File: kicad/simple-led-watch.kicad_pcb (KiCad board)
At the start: 2 copper layers, 32.5 x 32.5 mm, 156 parts, among them P1 BATTERY, P3 USB_OTG, Q1 MMBT3904, Q2 MMBT3904, SW1 SPST-4PIN, SW2 SPST-4PIN, SW3 SPST-4PIN, SW4 SPST-4PIN, U1 MCP73832, U2 TPS62736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

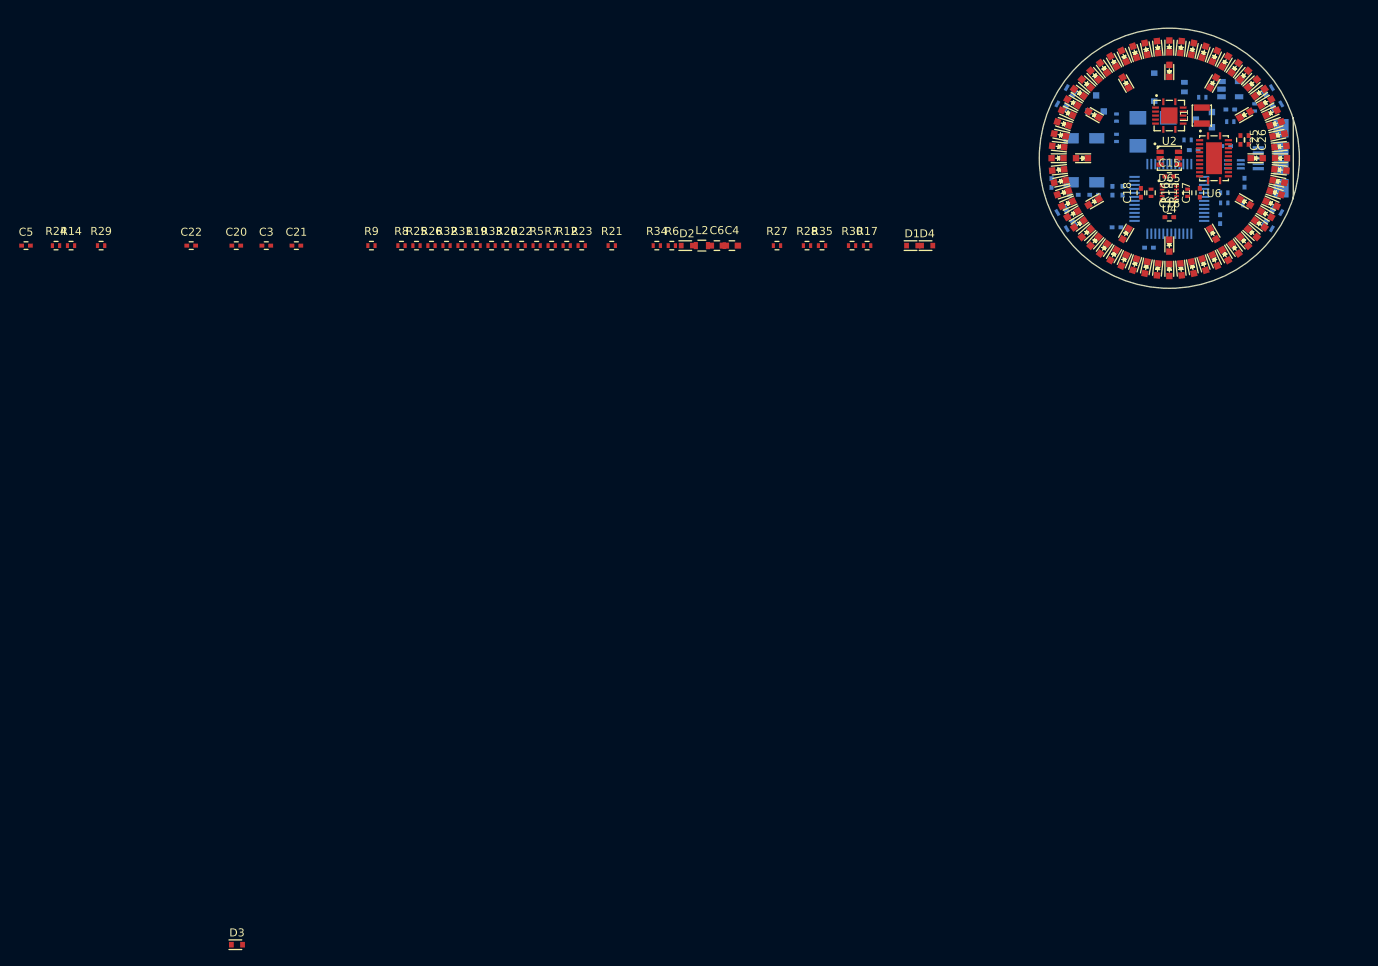
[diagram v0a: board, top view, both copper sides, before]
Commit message: Finished initial placement of all components
Got rid of several pullup resistors and unnecessary components.
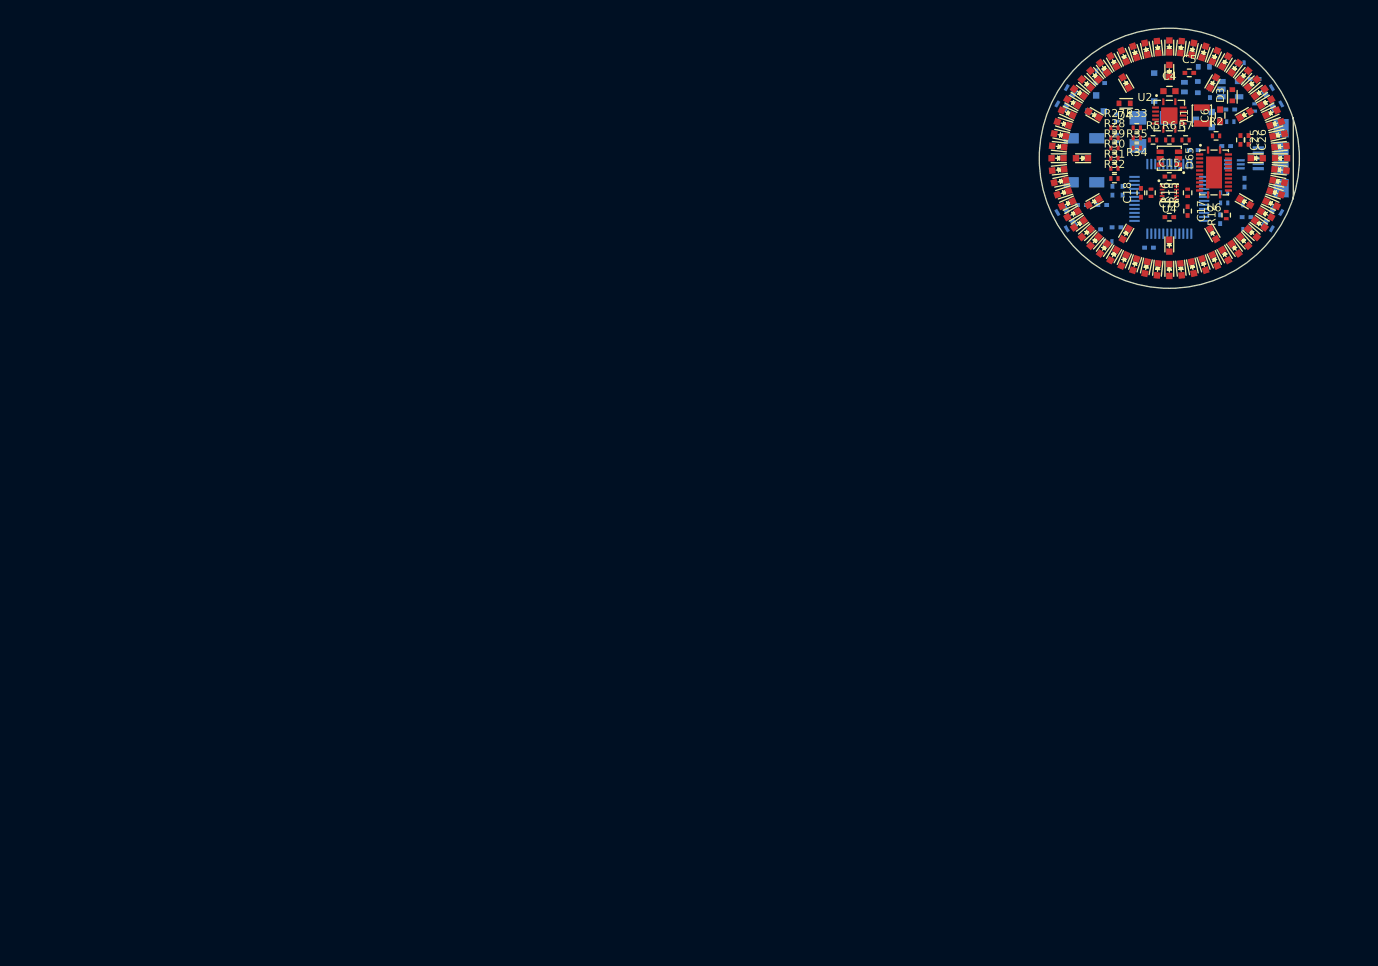
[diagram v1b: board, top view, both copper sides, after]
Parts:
- removed L2: 10u, Resistors_SMD:R_0603
- removed R14, R9: 0, Resistors_SMD:R_0402
- removed R17, R3: 10K, Resistors_SMD:R_0402
- removed R19, R21, R23, R25: R, Resistors_SMD:R_0402
- removed R8: 4M, Resistors_SMD:R_0402
- C20, C21, C22, C3, D1, D2: moved to B.Cu
- R2: value 10K -> 0; moved to F.Cu
- R20, R22, R24, R26: value R -> 0; moved to B.Cu
- R6: value 6M -> 0
- moved D3 163.6 mm to (173.0, 81.0), turned to 90 degrees
- moved C5 147.0 mm to (167.6, 78.2)
- moved R24 131.5 mm to (157.5, 99.3), turned to 180 degrees
- moved R29 127.3 mm to (158.2, 87.6)
- moved C20 126.3 mm to (174.8, 96.3)
- moved C3 119.5 mm to (170.2, 80.8), turned to 270 degrees
- moved C22 115.4 mm to (156.5, 79.5), turned to 180 degrees
- moved C21 100.0 mm to (156.0, 97.8), turned to 180 degrees
- moved R20 94.5 mm to (174.0, 77.0), turned to 180 degrees
- moved R22 90.6 mm to (174.8, 97.8)
- moved R26 86.4 mm to (156.5, 78.0), turned to 180 degrees
- moved R32 83.9 mm to (158.2, 91.4)
- moved R12 82.5 mm to (172.2, 96.0), turned to 90 degrees
- moved R31 82.2 mm to (158.2, 90.2)
- moved R33 82.0 mm to (161.0, 85.1)
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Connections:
- net /Control/STM32_OSC32_IN renamed /Control/STM32_OSC32+
- net /Control/STM32_OSC32_OUT renamed /Control/STM32_OSC32-
- C11 pad 1: /Control/STM32_VDDA -> +3V3
- C12 pad 1: /Control/STM32_VDDA -> +3V3
- C6 pad 1: +3V3 -> /Power Supply/+3.3V_REG_OUT
- D3 pad 1: +3V3 -> /Power Supply/+3.3V_REG_OUT
- L1 pad 2: +3V3 -> /Power Supply/+3.3V_REG_OUT
- R2 pad 2: /Control/CHG_STAT -> /Power Supply/+3.3V_REG_OUT
- R6 pad 1: /Power Supply/+3.3V_REG_VRDIV -> /Power Supply/+3.3V_REG_VOUT_SET
- R7 pad 1: /Power Supply/+3.3V_REG_VOUT_SET -> /Power Supply/+3.3V_REG_VOK_SET
- U2 pad 11: +3V3 -> /Power Supply/+3.3V_REG_OUT
- U2 pad 14: (no net) -> GND
- U2 pad 2: (no net) -> GND
- U2 pad 3: (no net) -> GND
- U2 pad 4: (no net) -> GND
- U3 pad 9: /Control/STM32_VDDA -> +3V3

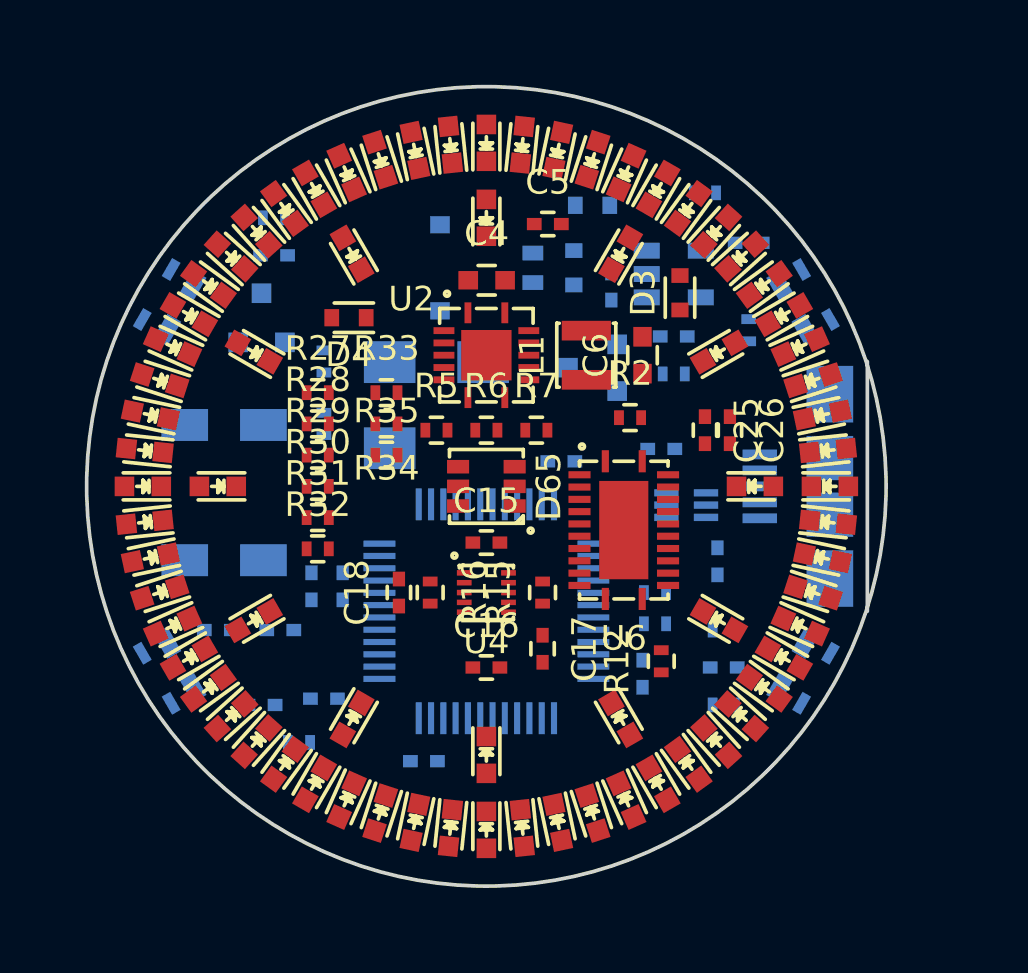
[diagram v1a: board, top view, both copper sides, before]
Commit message: Initial route of power and LED ring
I had to do the order swapping thing that I did on the last design
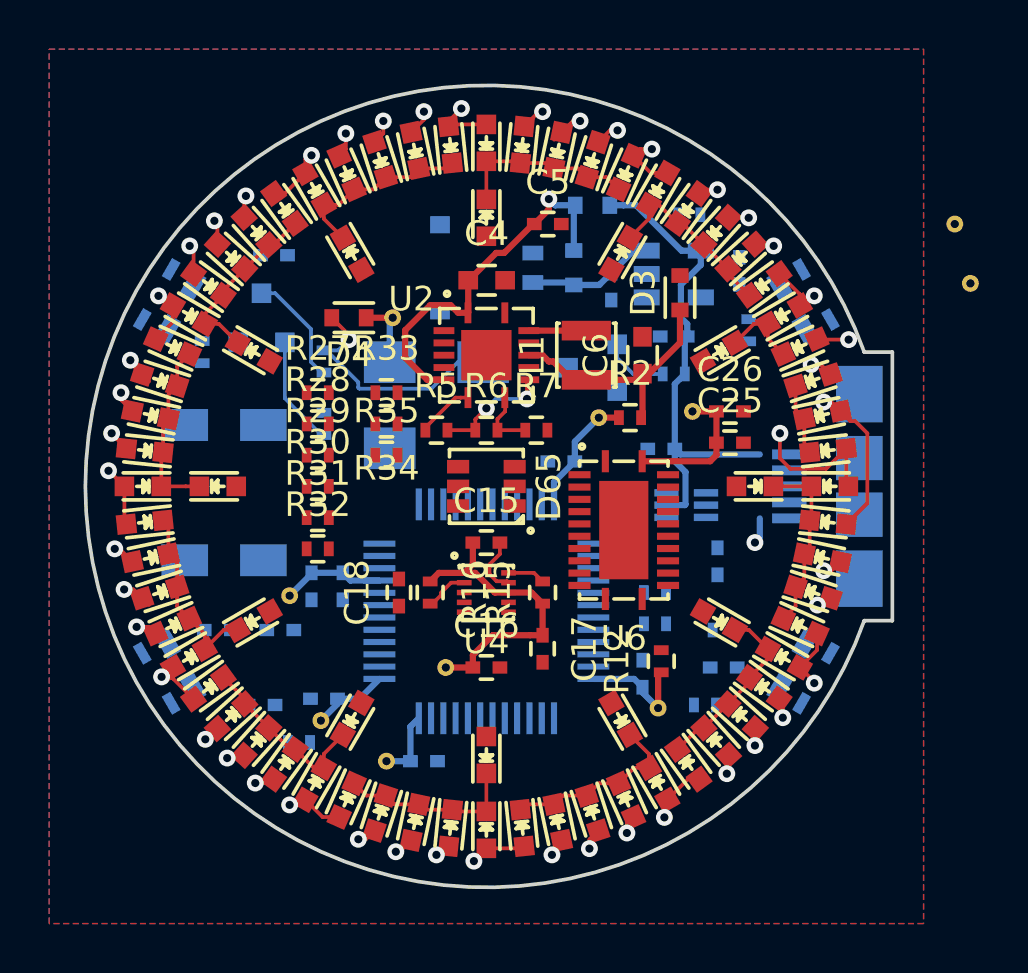
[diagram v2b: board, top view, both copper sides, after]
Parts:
- added REF**: 1PIN_VIA, simple-led-watch:1PIN_VIA, F.Cu at (169.7, 86.1)
- added REF**: 1PIN_VIA, simple-led-watch:1PIN_VIA, F.Cu at (161.3, 82.0)
- added REF**: 1PIN_VIA, simple-led-watch:1PIN_VIA, F.Cu at (184.8, 80.6)
- added REF**: 1PIN_VIA, simple-led-watch:1PIN_VIA, F.Cu at (184.2, 78.2)
- added REF**: 1PIN_VIA, simple-led-watch:1PIN_VIA, F.Cu at (172.1, 97.9)
- added REF**: 1PIN_VIA, simple-led-watch:1PIN_VIA, F.Cu at (161.0, 100.1)
- added REF**: 1PIN_VIA, simple-led-watch:1PIN_VIA, F.Cu at (158.4, 98.4)
- added REF**: 1PIN_VIA, simple-led-watch:1PIN_VIA, F.Cu at (163.4, 96.3)
- added REF**: 1PIN_VIA, simple-led-watch:1PIN_VIA, F.Cu at (157.1, 93.3)
- added REF**: 1PIN_VIA, simple-led-watch:1PIN_VIA, F.Cu at (173.5, 85.9)
- moved R26 6.19 mm to (153.5, 83.4), turned to 270 degrees
- moved C19 1.20 mm to (175.4, 80.1), turned to 270 degrees
- moved P3 1.20 mm to (180.3, 88.9)
- moved C25 1.14 mm to (175.0, 87.1), turned to 0 degrees
- moved R20 1.09 mm to (173.4, 77.9)
- moved C26 0.76 mm to (175.0, 85.9), turned to 0 degrees
- moved R22 0.76 mm to (174.0, 97.8)
- turned C22 to 0 degrees
- turned D66 to 270 degrees
- turned D67 to 240 degrees
- turned D68 to 210 degrees
- turned D69 to 180 degrees
- turned D70 to 150 degrees
- turned D71 to 120 degrees
- turned D72 to 90 degrees
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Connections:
- D10 pad 2: /LEDs/LED_A_R0 -> /LEDs/LED_A_R4
- D11 pad 2: /LEDs/LED_A_R1 -> /LEDs/LED_A_R3
- D13 pad 2: /LEDs/LED_A_R3 -> /LEDs/LED_A_R1
- D14 pad 2: /LEDs/LED_A_R4 -> /LEDs/LED_A_R0
- D20 pad 2: /LEDs/LED_A_R0 -> /LEDs/LED_A_R4
- D21 pad 2: /LEDs/LED_A_R1 -> /LEDs/LED_A_R3
- D23 pad 2: /LEDs/LED_A_R3 -> /LEDs/LED_A_R1
- D24 pad 2: /LEDs/LED_A_R4 -> /LEDs/LED_A_R0
- D30 pad 2: /LEDs/LED_A_R0 -> /LEDs/LED_A_R4
- D31 pad 2: /LEDs/LED_A_R1 -> /LEDs/LED_A_R3
- D33 pad 2: /LEDs/LED_A_R3 -> /LEDs/LED_A_R1
- D34 pad 2: /LEDs/LED_A_R4 -> /LEDs/LED_A_R0
- D40 pad 2: /LEDs/LED_A_R0 -> /LEDs/LED_A_R4
- D41 pad 2: /LEDs/LED_A_R1 -> /LEDs/LED_A_R3
- D43 pad 2: /LEDs/LED_A_R3 -> /LEDs/LED_A_R1
- D44 pad 2: /LEDs/LED_A_R4 -> /LEDs/LED_A_R0
- D50 pad 2: /LEDs/LED_A_R0 -> /LEDs/LED_A_R4
- D51 pad 2: /LEDs/LED_A_R1 -> /LEDs/LED_A_R3
- D53 pad 2: /LEDs/LED_A_R3 -> /LEDs/LED_A_R1
- D54 pad 2: /LEDs/LED_A_R4 -> /LEDs/LED_A_R0
- D60 pad 2: /LEDs/LED_A_R0 -> /LEDs/LED_A_R4
- D61 pad 2: /LEDs/LED_A_R1 -> /LEDs/LED_A_R3
- D63 pad 2: /LEDs/LED_A_R3 -> /LEDs/LED_A_R1
- D64 pad 2: /LEDs/LED_A_R4 -> /LEDs/LED_A_R0
- U5 pad 2: (no net) -> GND
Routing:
- net /LEDs/LED_A_R2: track 0.00 -> 103.8 mm, vias 0 -> 12
- net /LEDs/LED_A_R1: track 0.00 -> 101.2 mm, vias 0 -> 12
- net /LEDs/LED_A_R3: track 0.00 -> 99.5 mm, vias 0 -> 11
- net /LEDs/LED_A_R0: track 0.00 -> 96.2 mm, vias 0 -> 6
- net /LEDs/LED_A_R4: track 0.00 -> 94.4 mm, vias 0 -> 6
- net +3V3: track 0.00 -> 41.6 mm
- net /Power Supply/VUSB: track 0.00 -> 20.0 mm
- net /Power Supply/+3.3V_REG_SRC: track 0.00 -> 15.4 mm, vias 0 -> 1
- net /Power Supply/+3.3V_REG_OUT: track 0.00 -> 10.3 mm
- net Net-(D4-Pad2): track 0.00 -> 10.1 mm, vias 0 -> 1
- net /LEDs/LED_SEG5: track 0.00 -> 7.59 mm
- net /LEDs/LED_SEG8: track 0.00 -> 7.59 mm
- net /LEDs/LED_SEG11: track 0.00 -> 7.59 mm
- net /LEDs/LED_SEG6: track 0.00 -> 7.40 mm
- net /LEDs/LED_SEG9: track 0.00 -> 7.40 mm
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- added copper zone on In1.Cu, net +3V3
- added copper zone on B.Cu, net GND
- added copper zone on F.Cu, net GND
- added copper zone on In2.Cu, net GND
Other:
- board size 32.5 x 32.5 mm -> 32.8 x 32.6 mm
- copper layers 2 -> 4
- net class Default: clearance 0.2 -> 0.1524; trace_width 0.25 -> 0.1524
- net class Power added: clearance 0.1524, trace_width 0.254, via_dia 0.6858, via_drill 0.3302
- rule trace_clearance: 0.2 -> 0.1524
- board text added: "Notes: Vias MUST be tented since we put them beneath some metal components"

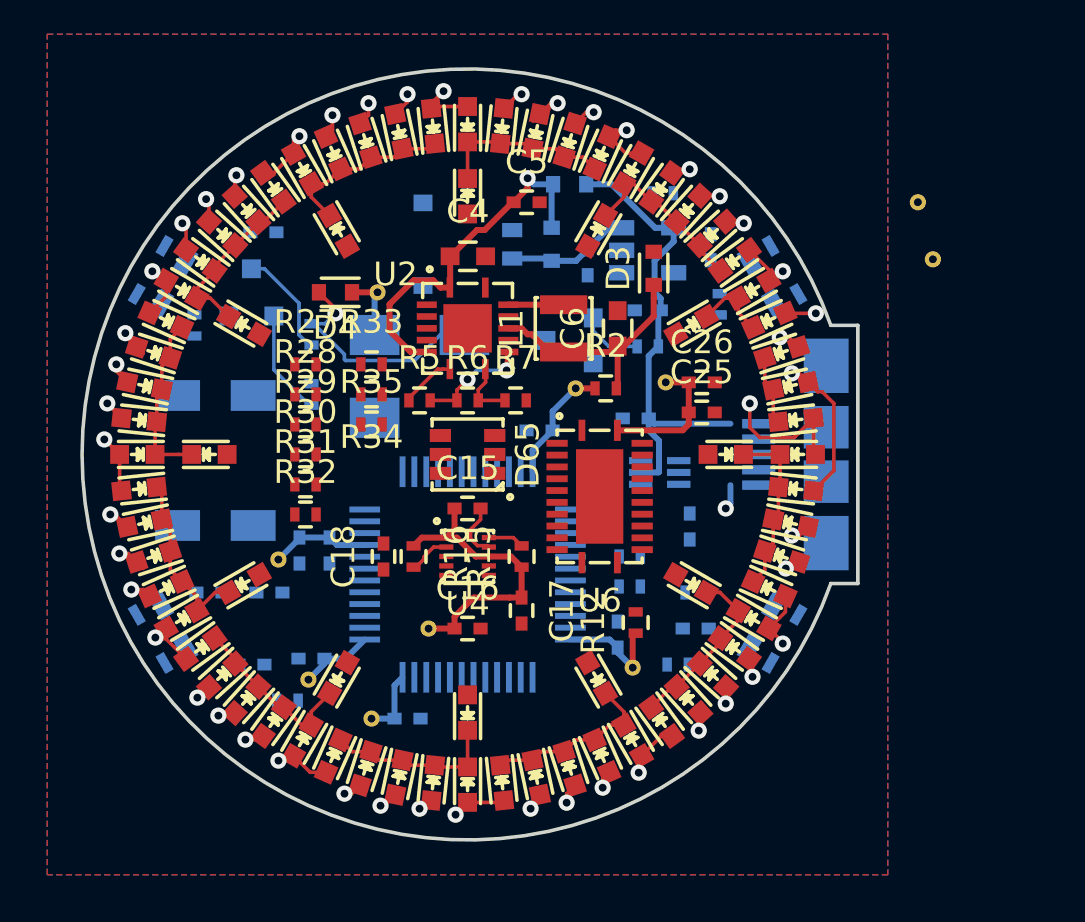
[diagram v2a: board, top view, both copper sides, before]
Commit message: Routed most of the board, except buttons and interrupts
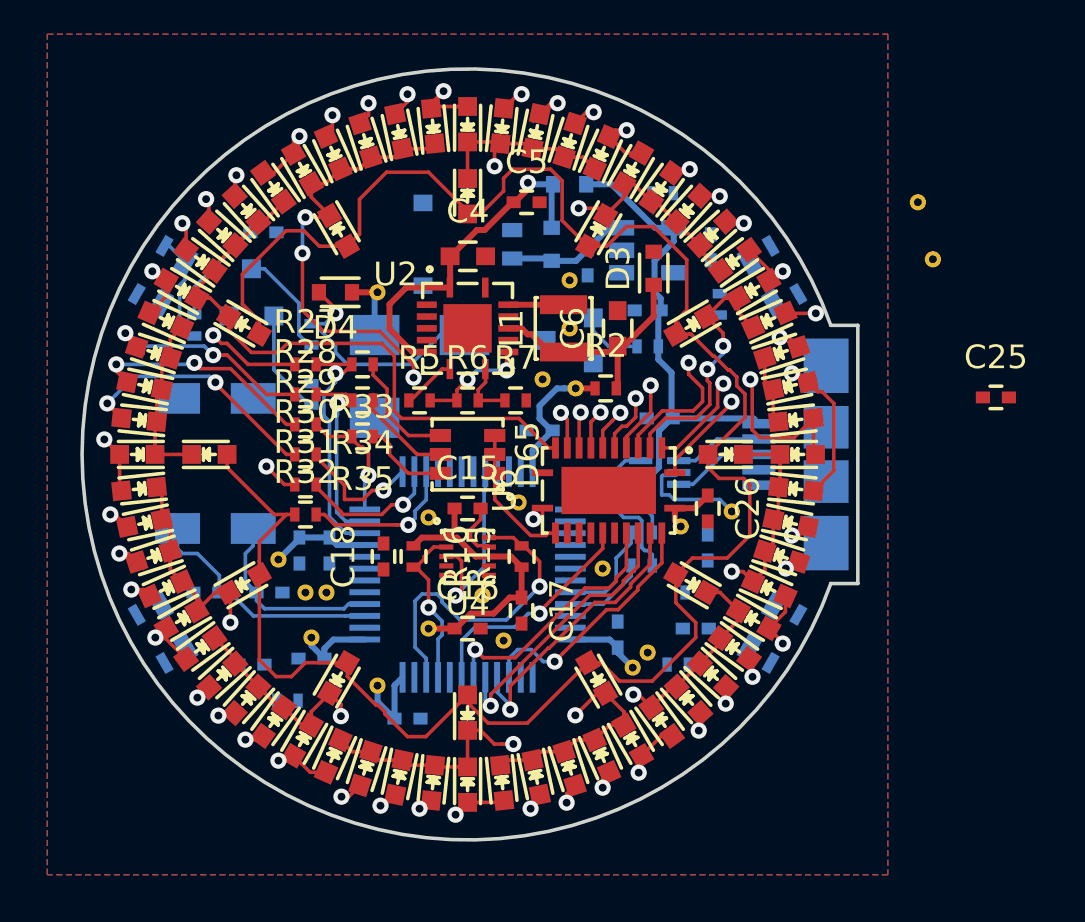
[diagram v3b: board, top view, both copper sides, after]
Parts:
- removed R12: 10K, Resistors_SMD:R_0402
- added REF**: 1PIN_VIA, simple-led-watch:1PIN_VIA, F.Cu at (172.7, 97.3)
- added REF**: 1PIN_VIA, simple-led-watch:1PIN_VIA, F.Cu at (167.3, 90.9)
- added REF**: 1PIN_VIA, simple-led-watch:1PIN_VIA, F.Cu at (159.1, 94.7)
- added REF**: 1PIN_VIA, simple-led-watch:1PIN_VIA, F.Cu at (158.2, 94.7)
- added REF**: 1PIN_VIA, simple-led-watch:1PIN_VIA, F.Cu at (170.8, 93.7)
- added REF**: 1PIN_VIA, simple-led-watch:1PIN_VIA, F.Cu at (163.4, 91.6)
- added REF**: 1PIN_VIA, simple-led-watch:1PIN_VIA, F.Cu at (166.6, 96.8)
- added REF**: 1PIN_VIA, simple-led-watch:1PIN_VIA, F.Cu at (165.7, 94.9)
- added REF**: 1PIN_VIA, simple-led-watch:1PIN_VIA, F.Cu at (169.4, 81.5)
- added REF**: 1PIN_VIA, simple-led-watch:1PIN_VIA, F.Cu at (169.4, 83.6)
- added REF**: 1PIN_VIA, simple-led-watch:1PIN_VIA, F.Cu at (168.3, 85.7)
- added REF**: 1PIN_VIA, simple-led-watch:1PIN_VIA, F.Cu at (176.3, 91.3)
- moved C25 12.5 mm to (187.5, 86.5)
- moved REF** 6.13 mm to (174.1, 91.9)
- moved C26 5.34 mm to (175.3, 91.2), turned to 270 degrees
- moved C13 2.67 mm to (154.1, 94.7), turned to 180 degrees
- moved C14 2.54 mm to (156.7, 94.7), turned to 0 degrees
- moved REF** 1.78 mm to (158.5, 96.6)
- moved REF** 1.42 mm to (161.3, 98.7)
- moved C27 1.17 mm to (175.3, 92.8)
- moved R10 1.14 mm to (172.5, 92.2)
- moved R11 1.02 mm to (172.5, 93.6)
- moved C2 1.02 mm to (173.2, 87.4)
- moved R35 0.64 mm to (160.7, 88.1), turned to 180 degrees
- moved R34 0.46 mm to (160.7, 86.6)
- moved U6 0.46 mm to (171.1, 90.4), turned to 180 degrees
- moved R33 0.38 mm to (160.7, 85.1), turned to 180 degrees
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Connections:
- Y1 pad 1: /Control/STM32_OSC32+ -> /Control/STM32_OSC32-
- Y1 pad 2: /Control/STM32_OSC32- -> /Control/STM32_OSC32+
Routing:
- net /LEDs/LED_A_R5: track 0.00 -> 87.4 mm
- net /LEDs/LED_SEG8: track 7.59 -> 42.7 mm, vias 0 -> 2
- net /LEDs/LED_SEG7: track 7.39 -> 36.6 mm, vias 0 -> 2
- net /LEDs/LED_SEG0: track 7.40 -> 30.6 mm, vias 0 -> 2
- net /LEDs/LED_SEG6: track 7.40 -> 30.1 mm, vias 0 -> 2
- net /LEDs/LED_SEG5: track 7.59 -> 28.4 mm, vias 0 -> 2
- net /LEDs/LED_SEG11: track 7.59 -> 27.7 mm, vias 0 -> 4
- net /LEDs/LED_SEG4: track 7.39 -> 26.2 mm, vias 0 -> 2
- net /LEDs/LED_SEG1: track 7.39 -> 25.6 mm, vias 0 -> 2
- net /LEDs/LED_SEG10: track 7.39 -> 25.5 mm
- net /LEDs/LED_SEG3: track 7.40 -> 23.8 mm, vias 0 -> 2
- net /Control/LED_C_MUX1: track 0.00 -> 12.0 mm, vias 0 -> 1
- net /Control/I2C_SDA: track 1.53 -> 13.6 mm, vias 0 -> 1
- net /Control/LED_C_MUX2: track 0.00 -> 11.7 mm, vias 0 -> 1
- net /Control/LED_C_MUX3: track 0.00 -> 10.9 mm, vias 0 -> 1
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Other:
- rule pad_to_mask_clearance: 0.2 -> 0.1524
